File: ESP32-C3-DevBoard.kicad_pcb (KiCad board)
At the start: 2 copper layers, 25.4 x 26 mm, 21 parts, among them J1 USB_C_Receptacle_USB2.0_16P, J2 Conn_01x10, J3 Conn_01x10, SW1 SW_Push, SW2 SW_Push, U1 ESP32-C3-WROOM-02, U3 RT9080-33GJ5

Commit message: solder jumper fix
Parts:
- JP1: value Jumper_2_Open -> SolderJumper_2_Open
- JP2: value Jumper_2_Bridged -> SolderJumper_2_Bridged

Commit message: show reference number
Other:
- board text removed: "5V→3V3"
- board text removed: "VBUS=5V"
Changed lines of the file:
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@@
 		(tags "net tie solder jumper bridged")
 		(property "Reference" "JP2"
-			(at 0 1.8 0)
-			(layer "B.SilkS")
-			(hide yes)
-			(effects
-				(font
-					(size 0.8 0.8)
-					(thickness 0.15)
+			(at 0 1.905 0)
+			(layer "B.SilkS")
+			(effects
+				(font
+					(size 1 1)
+					(thickness 0.2)
 				)
 				(justify mirror)
@@
 		(tags "solder jumper open")
 		(property "Reference" "JP1"
-			(at 0 1.8 0)
-			(layer "B.SilkS")
-			(hide yes)
-			(effects
-				(font
-					(size 0.8 0.8)
-					(thickness 0.15)
+			(at 0 1.905 0)
+			(layer "B.SilkS")
+			(effects
+				(font
+					(size 1 1)
+					(thickness 0.2)
 				)
 				(justify mirror)
@@
 		(layer "Edge.Cuts")
 	)
-	(gr_text "VBUS=5V"
-		(at 150.495 111.76 0)
-		(layer "B.SilkS")
-		(effects
-			(font
-				(size 0.8 0.8)
-				(thickness 0.15)
-			)
-			(justify mirror)
-		)
-	)
-	(gr_text "5V→3V3"
-		(at 141.605 111.76 0)
-		(layer "B.SilkS")
-		(effects
-			(font
-				(size 0.8 0.8)
-				(thickness 0.15)
-			)
-			(justify mirror)
-		)
-	)
 	(gr_text "10"

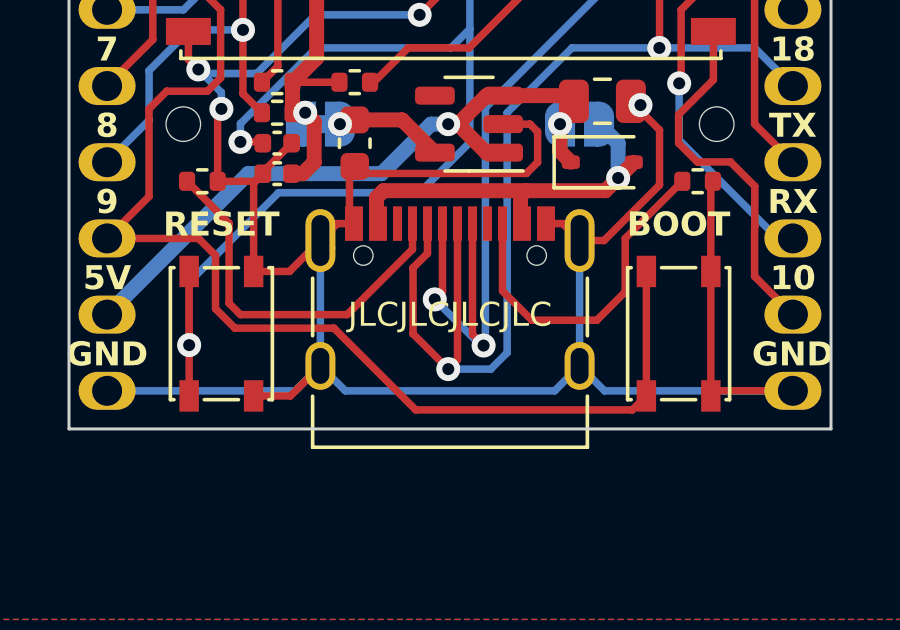
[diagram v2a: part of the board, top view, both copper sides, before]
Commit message: jlcpcb offset fix
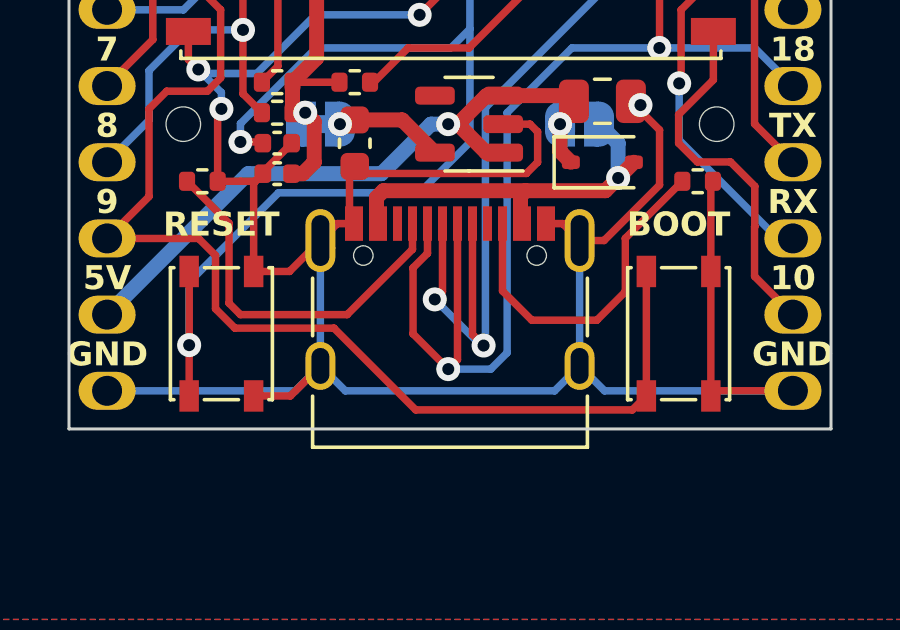
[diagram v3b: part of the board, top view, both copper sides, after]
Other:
- board text removed: "JLCJLCJLCJLC"
